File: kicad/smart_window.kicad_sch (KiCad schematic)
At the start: 15 parts, among them J1 PROG, J7 I2C

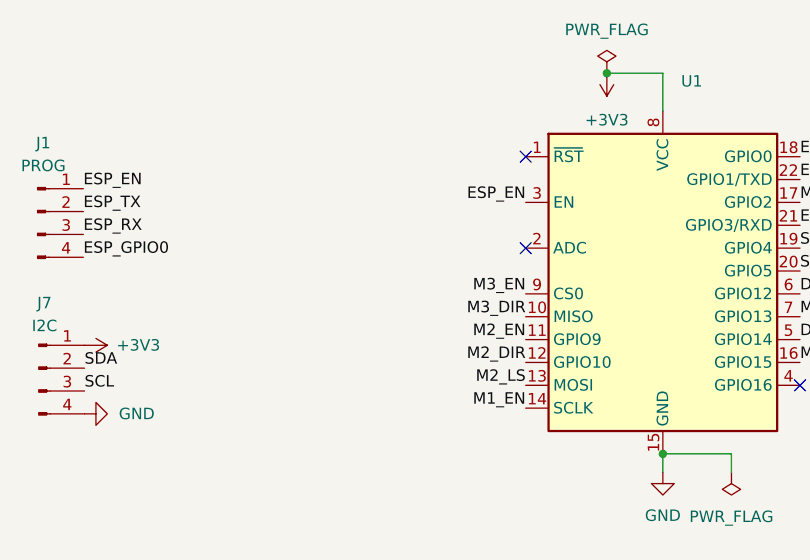
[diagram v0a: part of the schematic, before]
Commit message: добавил фотосенсор
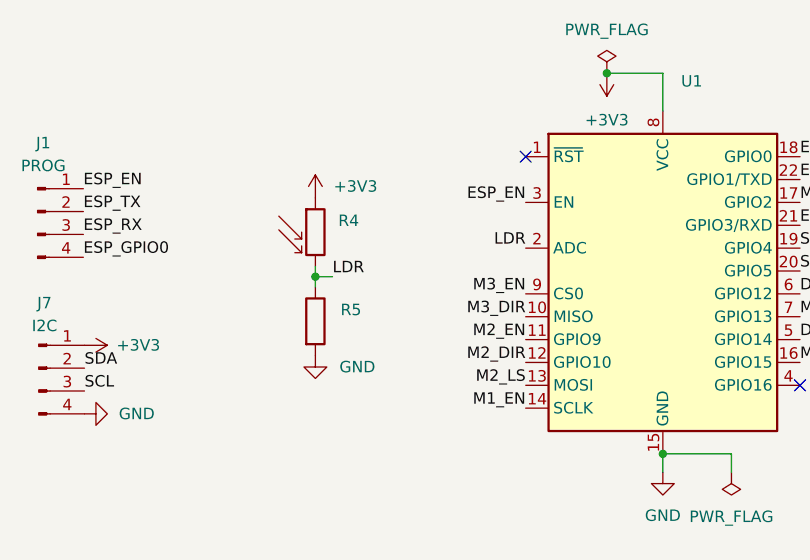
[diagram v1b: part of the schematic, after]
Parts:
- added R4: (no value), symbol Sensor_Optical:A9050
- added R5: (no value), symbol Device:R
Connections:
- net +3V3: now also R4.1
- net GND: now also R5.2
- net LDR: now reaches U1.2 (ADC)
- net LDR: now also R4.2, R5.1
- no-connect marks 3 -> 2
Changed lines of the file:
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@@
 (kicad_sch (version 20211123) (generator eeschema)
   (paper "A4")
+  (junction (at 55.626 46.609) (diameter 0) (color 0 0 0 0)
+  )
   (junction (at 88.011 24.003) (diameter 0) (color 0 0 0 0)
   )
@@
   )
   (no_connect (at 78.994 33.274))
-  (no_connect (at 78.994 43.434))
   (no_connect (at 109.474 58.674))
+  (wire (pts (xy 55.626 45.466) (xy 55.626 46.609))
+    (stroke (width 0) (type default) (color 0 0 0 0))
+  )
   (wire (pts (xy 155.956 50.292) (xy 162.433 50.292))
     (stroke (width 0) (type default) (color 0 0 0 0))
@@
     (stroke (width 0) (type default) (color 0 0 0 0))
   )
+  (wire (pts (xy 55.626 46.609) (xy 55.626 47.752))
+    (stroke (width 0) (type default) (color 0 0 0 0))
+  )
   (wire (pts (xy 124.587 88.519) (xy 128.651 88.519))
     (stroke (width 0) (type default) (color 0 0 0 0))
@@
     (stroke (width 0) (type default) (color 0 0 0 0))
   )
+  (wire (pts (xy 55.626 46.609) (xy 57.531 46.609))
+    (stroke (width 0) (type default) (color 0 0 0 0))
+  )
   (wire (pts (xy 124.587 112.903) (xy 128.651 112.903))
     (stroke (width 0) (type default) (color 0 0 0 0))
@@
     (effects (font (size 1.27 1.27)) (justify right bottom))
   )
+  (label "LDR" (at 57.531 46.609 0)
+    (effects (font (size 1.27 1.27)) (justify left bottom))
+  )
   (label "M2_LS" (at 128.651 97.79 180)
     (effects (font (size 1.27 1.27)) (justify right bottom))
@@
   (label "M1_LS" (at 109.474 56.134 0)
     (effects (font (size 1.27 1.27)) (justify left bottom))
+  )
+  (label "LDR" (at 78.994 43.434 180)
+    (effects (font (size 1.27 1.27)) (justify right bottom))
   )
   (label "M3_LS" (at 109.474 51.054 0)
@@
     )
     (pin "1")
+  )
+  (symbol (lib_id "power:GND") (at 55.626 55.372 0) (unit 1)
+    (in_bom yes) (on_board yes) (fields_autoplaced)
+    (property "Reference" "#PWR011" (id 0) (at 55.626 61.722 0)
+      (effects (font (size 1.27 1.27)) hide)
+    )
+    (property "Value" "GND" (id 1) (at 58.293 56.6419 0)
+      (effects (font (size 1.27 1.27)) (justify left))
+    )
+    (property "Footprint" "" (id 2) (at 55.626 55.372 0)
+      (effects (font (size 1.27 1.27)) hide)
+    )
+    (property "Datasheet" "" (id 3) (at 55.626 55.372 0)
+      (effects (font (size 1.27 1.27)) hide)
+    )
+    (pin "1")
+  )
+  (symbol (lib_id "Device:R") (at 55.626 51.562 0) (unit 1)
+    (in_bom yes) (on_board yes) (fields_autoplaced)
+    (property "Reference" "R5" (id 0) (at 58.42 50.2919 0)
+      (effects (font (size 1.27 1.27)) (justify left))
+    )
+    (property "Value" "" (id 1) (at 58.42 52.8319 0)
+      (effects (font (size 1.27 1.27)) (justify left))
+    )
+    (property "Footprint" "" (id 2) (at 53.848 51.562 90)
+      (effects (font (size 1.27 1.27)) hide)
+    )
+    (property "Datasheet" "~" (id 3) (at 55.626 51.562 0)
+      (effects (font (size 1.27 1.27)) hide)
+    )
+    (pin "1")
+    (pin "2")
   )
   (symbol (lib_id "Connector:Conn_01x02_Male") (at 133.731 110.363 0) (mirror y) (unit 1)
@@
     (pin "2")
   )
+  (symbol (lib_id "power:+3V3") (at 55.626 37.846 0) (unit 1)
+    (in_bom yes) (on_board yes) (fields_autoplaced)
+    (property "Reference" "#PWR08" (id 0) (at 55.626 41.656 0)
+      (effects (font (size 1.27 1.27)) hide)
+    )
+    (property "Value" "+3V3" (id 1) (at 57.658 36.5759 0)
+      (effects (font (size 1.27 1.27)) (justify left))
+    )
+    (property "Footprint" "" (id 2) (at 55.626 37.846 0)
+      (effects (font (size 1.27 1.27)) hide)
+    )
+    (property "Datasheet" "" (id 3) (at 55.626 37.846 0)
+      (effects (font (size 1.27 1.27)) hide)
+    )
+    (pin "1")
+  )
   (symbol (lib_id "Connector:Conn_01x04_Male") (at 24.765 39.37 0) (unit 1)
     (in_bom yes) (on_board yes) (fields_autoplaced)
@@
     (pin "3")
     (pin "4")
+  )
+  (symbol (lib_id "Sensor_Optical:A9050") (at 55.626 41.656 0) (unit 1)
+    (in_bom yes) (on_board yes) (fields_autoplaced)
+    (property "Reference" "R4" (id 0) (at 58.166 40.3859 0)
+      (effects (font (size 1.27 1.27)) (justify left))
+    )
+    (property "Value" "" (id 1) (at 58.166 42.9259 0)
+      (effects (font (size 1.27 1.27)) (justify left))
+    )
+    (property "Footprint" "" (id 2) (at 60.071 41.656 90)
+      (effects (font (size 1.27 1.27)) hide)
+    )
+    (property "Datasheet" "http://cdn-reichelt.de/documents/datenblatt/A500/A90xxxx%23PE.pdf" (id 3) (at 55.626 42.926 0)
+      (effects (font (size 1.27 1.27)) hide)
+    )
+    (pin "1")
+    (pin "2")
   )
   (symbol (lib_id "Connector:Conn_01x02_Male") (at 155.067 20.193 0) (mirror y) (unit 1)
@@
       (reference "#PWR07") (unit 1) (value "GND") (footprint "")
     )
+    (path "/70651bab-fd48-4e85-b84c-55639ba11578"
+      (reference "#PWR08") (unit 1) (value "+3V3") (footprint "")
+    )
     (path "/57e793a7-1996-4f00-92db-a3562d1780dc"
       (reference "#PWR09") (unit 1) (value "GND") (footprint "")
@@
       (reference "#PWR010") (unit 1) (value "GND") (footprint "")
     )
+    (path "/3805e47f-de2b-4f83-86bb-b738762f423a"
+      (reference "#PWR011") (unit 1) (value "GND") (footprint "")
+    )
     (path "/2e774311-d5bd-4ef6-ad7a-5f00d4153613"
       (reference "#PWR014") (unit 1) (value "+3V3") (footprint "")
@@
       (reference "R3") (unit 1) (value "50") (footprint "Resistor_SMD:R_0805_2012Metric")
     )
+    (path "/8407e94d-ce93-4e05-96a2-52621e9e6eb2"
+      (reference "R4") (unit 1) (value "A9050") (footprint "OptoDevice:R_LDR_5.0x4.1mm_P3mm_Vertical")
+    )
+    (path "/3d7ad9f7-d5b6-454d-8f0a-1bda65cbec76"
+      (reference "R5") (unit 1) (value "500") (footprint "Resistor_SMD:R_0805_2012Metric")
+    )
     (path "/c8e0800a-7e51-46cc-9c63-1120638a3624/0d5cf8e3-75e7-46ab-b654-c6274a5de87d"

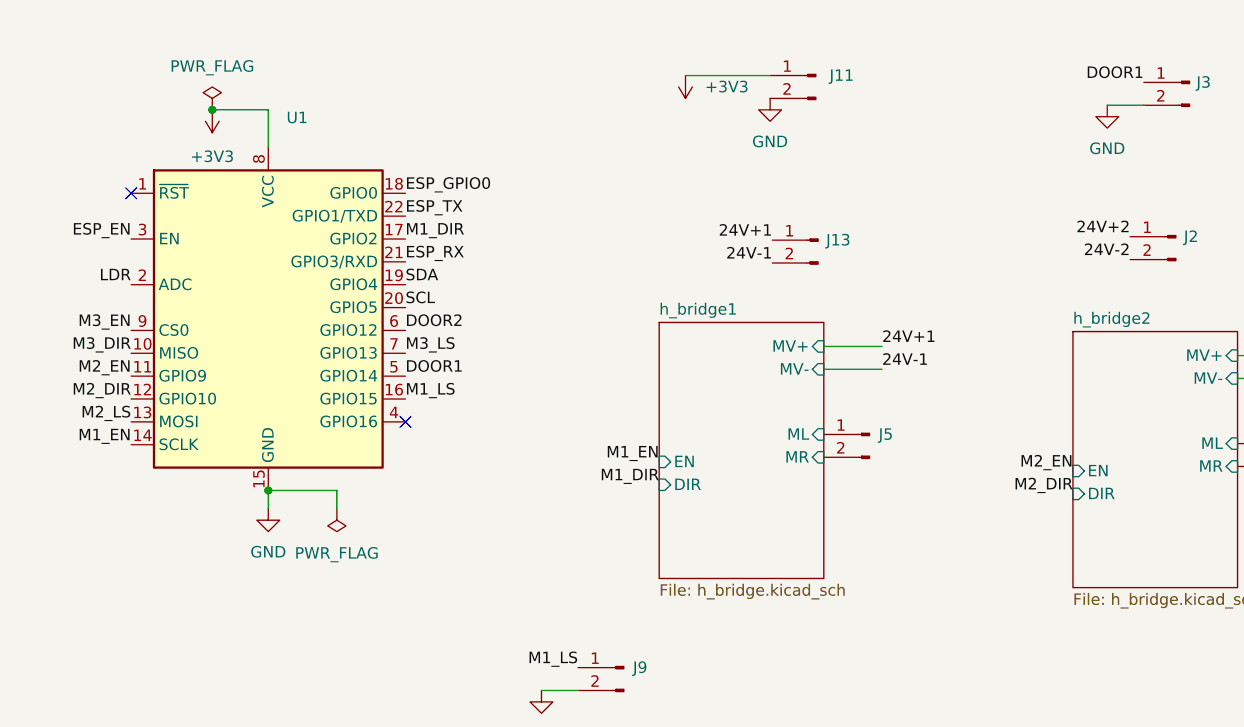
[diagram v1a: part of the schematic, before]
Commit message: добавлен DC-DC преобразователь для питания 3В от БП двигателя
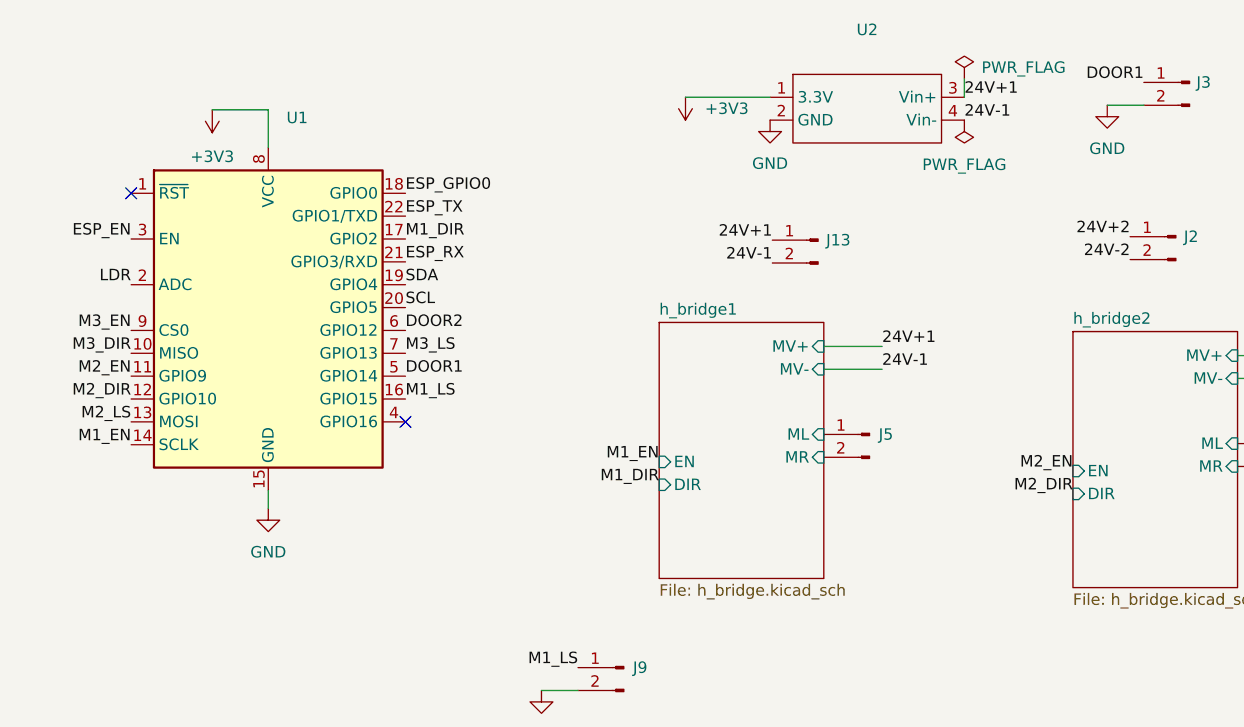
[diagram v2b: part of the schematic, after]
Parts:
- removed J11: (no value), symbol Connector:Conn_01x02_Male
- added U2: (no value), Power Modules:MP1584EN, symbol Power Modules:MP1584EN 3.3V
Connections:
- net +3V3: now also U2.1 (3.3V)
- net 24V+1: now also U2.3 (Vin+)
- net 24V-1: now also U2.4 (Vin-)
- net GND: now also U2.2 (GND)
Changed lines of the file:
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@@
   (junction (at 55.626 46.609) (diameter 0) (color 0 0 0 0)
-  )
-  (junction (at 88.011 24.003) (diameter 0) (color 0 0 0 0)
-  )
-  (junction (at 94.234 66.294) (diameter 0) (color 0 0 0 0)
   )
   (no_connect (at 78.994 33.274))
@@
     (stroke (width 0) (type default) (color 0 0 0 0))
   )
+  (wire (pts (xy 171.577 20.574) (xy 171.577 22.606))
+    (stroke (width 0) (type default) (color 0 0 0 0))
+  )
   (wire (pts (xy 155.956 50.292) (xy 162.433 50.292))
     (stroke (width 0) (type default) (color 0 0 0 0))
@@
     (stroke (width 0) (type default) (color 0 0 0 0))
   )
-  (wire (pts (xy 140.589 20.193) (xy 149.987 20.193))
+  (wire (pts (xy 140.589 22.606) (xy 149.987 22.606))
     (stroke (width 0) (type default) (color 0 0 0 0))
   )
@@
     (stroke (width 0) (type default) (color 0 0 0 0))
   )
-  (wire (pts (xy 101.854 66.294) (xy 94.234 66.294))
-    (stroke (width 0) (type default) (color 0 0 0 0))
-  )
-  (wire (pts (xy 101.854 68.326) (xy 101.854 66.294))
-    (stroke (width 0) (type default) (color 0 0 0 0))
-  )
   (wire (pts (xy 55.626 46.609) (xy 57.531 46.609))
     (stroke (width 0) (type default) (color 0 0 0 0))
@@
   (label "M3_DIR" (at 224.028 66.929 180)
     (effects (font (size 1.27 1.27)) (justify right bottom))
+  )
+  (label "24V+1" (at 171.577 22.606 0)
+    (effects (font (size 1.27 1.27)) (justify left bottom))
+  )
+  (label "24V-1" (at 171.577 25.146 0)
+    (effects (font (size 1.27 1.27)) (justify left bottom))
   )
   (label "LDR" (at 57.531 46.609 0)
@@
     (pin "1")
   )
-  (symbol (lib_id "power:GND") (at 149.987 22.733 0) (unit 1)
-    (in_bom yes) (on_board yes) (fields_autoplaced)
-    (property "Reference" "#PWR017" (id 0) (at 149.987 29.083 0)
-      (effects (font (size 1.27 1.27)) hide)
-    )
-    (property "Value" "GND" (id 1) (at 149.987 27.559 0))
-    (property "Footprint" "" (id 2) (at 149.987 22.733 0)
-      (effects (font (size 1.27 1.27)) hide)
-    )
-    (property "Datasheet" "" (id 3) (at 149.987 22.733 0)
-      (effects (font (size 1.27 1.27)) hide)
-    )
-    (pin "1")
-  )
-  (symbol (lib_id "power:PWR_FLAG") (at 101.854 68.326 180) (unit 1)
-    (in_bom yes) (on_board yes) (fields_autoplaced)
-    (property "Reference" "#FLG0101" (id 0) (at 101.854 70.231 0)
-      (effects (font (size 1.27 1.27)) hide)
-    )
-    (property "Value" "PWR_FLAG" (id 1) (at 101.854 73.279 0))
-    (property "Footprint" "" (id 2) (at 101.854 68.326 0)
-      (effects (font (size 1.27 1.27)) hide)
-    )
-    (property "Datasheet" "~" (id 3) (at 101.854 68.326 0)
+  (symbol (lib_id "power:GND") (at 149.987 25.146 0) (unit 1)
+    (in_bom yes) (on_board yes) (fields_autoplaced)
+    (property "Reference" "#PWR017" (id 0) (at 149.987 31.496 0)
+      (effects (font (size 1.27 1.27)) hide)
+    )
+    (property "Value" "GND" (id 1) (at 149.987 29.972 0))
+    (property "Footprint" "" (id 2) (at 149.987 25.146 0)
+      (effects (font (size 1.27 1.27)) hide)
+    )
+    (property "Datasheet" "" (id 3) (at 149.987 25.146 0)
       (effects (font (size 1.27 1.27)) hide)
     )
@@
     )
     (property "Datasheet" "" (id 3) (at 124.587 88.519 0)
+      (effects (font (size 1.27 1.27)) hide)
+    )
+    (pin "1")
+  )
+  (symbol (lib_id "power:PWR_FLAG") (at 171.577 20.574 0) (unit 1)
+    (in_bom yes) (on_board yes) (fields_autoplaced)
+    (property "Reference" "#FLG0101" (id 0) (at 171.577 18.669 0)
+      (effects (font (size 1.27 1.27)) hide)
+    )
+    (property "Value" "PWR_FLAG" (id 1) (at 173.482 19.3039 0)
+      (effects (font (size 1.27 1.27)) (justify left))
+    )
+    (property "Footprint" "" (id 2) (at 171.577 20.574 0)
+      (effects (font (size 1.27 1.27)) hide)
+    )
+    (property "Datasheet" "~" (id 3) (at 171.577 20.574 0)
       (effects (font (size 1.27 1.27)) hide)
     )
@@
     )
     (pin "1")
+  )
+  (symbol (lib_id "Power Modules:MP1584EN 3.3V") (at 160.147 23.876 0) (unit 1)
+    (in_bom yes) (on_board yes) (fields_autoplaced)
+    (property "Reference" "U2" (id 0) (at 160.782 15.113 0))
+    (property "Value" "" (id 1) (at 160.782 17.653 0))
+    (property "Footprint" "Power Modules:MP1584EN" (id 2) (at 149.987 22.606 0)
+      (effects (font (size 1.27 1.27)) hide)
+    )
+    (property "Datasheet" "https://aliexpress.ru/item/1005003880292594.html" (id 3) (at 160.147 32.766 0)
+      (effects (font (size 1.27 1.27)) hide)
+    )
+    (pin "1")
+    (pin "2")
+    (pin "3")
+    (pin "4")
   )
   (symbol (lib_id "RF_Module:ESP-12F") (at 94.234 48.514 0) (unit 1)
@@
     (pin "2")
   )
-  (symbol (lib_id "Connector:Conn_01x02_Male") (at 155.067 20.193 0) (mirror y) (unit 1)
-    (in_bom yes) (on_board yes) (fields_autoplaced)
-    (property "Reference" "J11" (id 0) (at 156.591 20.1929 0)
-      (effects (font (size 1.27 1.27)) (justify right))
-    )
-    (property "Value" "" (id 1) (at 156.591 22.7329 0)
-      (effects (font (size 1.27 1.27)) (justify right))
-    )
-    (property "Footprint" "" (id 2) (at 155.067 20.193 0)
-      (effects (font (size 1.27 1.27)) hide)
-    )
-    (property "Datasheet" "~" (id 3) (at 155.067 20.193 0)
-      (effects (font (size 1.27 1.27)) hide)
-    )
-    (pin "1")
-    (pin "2")
-  )
   (symbol (lib_id "power:GND") (at 29.972 61.849 90) (unit 1)
     (in_bom yes) (on_board yes) (fields_autoplaced)
@@
     (pin "1")
   )
-  (symbol (lib_id "power:PWR_FLAG") (at 88.011 24.003 0) (unit 1)
-    (in_bom yes) (on_board yes) (fields_autoplaced)
-    (property "Reference" "#FLG01" (id 0) (at 88.011 22.098 0)
-      (effects (font (size 1.27 1.27)) hide)
-    )
-    (property "Value" "PWR_FLAG" (id 1) (at 88.011 19.177 0))
-    (property "Footprint" "" (id 2) (at 88.011 24.003 0)
-      (effects (font (size 1.27 1.27)) hide)
-    )
-    (property "Datasheet" "~" (id 3) (at 88.011 24.003 0)
+  (symbol (lib_id "power:PWR_FLAG") (at 171.577 25.146 180) (unit 1)
+    (in_bom yes) (on_board yes) (fields_autoplaced)
+    (property "Reference" "#FLG0102" (id 0) (at 171.577 27.051 0)
+      (effects (font (size 1.27 1.27)) hide)
+    )
+    (property "Value" "PWR_FLAG" (id 1) (at 171.577 30.099 0))
+    (property "Footprint" "" (id 2) (at 171.577 25.146 0)
+      (effects (font (size 1.27 1.27)) hide)
+    )
+    (property "Datasheet" "~" (id 3) (at 171.577 25.146 0)
       (effects (font (size 1.27 1.27)) hide)
     )
@@
     (pin "2")
   )
-  (symbol (lib_id "power:+3V3") (at 140.589 20.193 180) (unit 1)
+  (symbol (lib_id "power:+3V3") (at 140.589 22.606 180) (unit 1)
     (in_bom yes) (on_board yes)
-    (property "Reference" "#PWR016" (id 0) (at 140.589 16.383 0)
-      (effects (font (size 1.27 1.27)) hide)
-    )
-    (property "Value" "+3V3" (id 1) (at 142.748 21.4629 0)
-      (effects (font (size 1.27 1.27)) (justify right))
-    )
-    (property "Footprint" "" (id 2) (at 140.589 20.193 0)
-      (effects (font (size 1.27 1.27)) hide)
-    )
-    (property "Datasheet" "" (id 3) (at 140.589 20.193 0)
+    (property "Reference" "#PWR016" (id 0) (at 140.589 18.796 0)
+      (effects (font (size 1.27 1.27)) hide)
+    )
+    (property "Value" "+3V3" (id 1) (at 142.748 23.8759 0)
+      (effects (font (size 1.27 1.27)) (justify right))
+    )
+    (property "Footprint" "" (id 2) (at 140.589 22.606 0)
+      (effects (font (size 1.27 1.27)) hide)
+    )
+    (property "Datasheet" "" (id 3) (at 140.589 22.606 0)
       (effects (font (size 1.27 1.27)) hide)
     )
@@
   )
   (symbol_instances
-    (path "/bc9dccb7-f29e-45b0-9679-592bb5c286c7"
-      (reference "#FLG01") (unit 1) (value "PWR_FLAG") (footprint "")
-    )
-    (path "/33104779-36fd-476d-a6d8-6e7021545d3d"
+    (path "/36634bbd-43fa-4289-adf5-4285d5ab34e1"
       (reference "#FLG0101") (unit 1) (value "PWR_FLAG") (footprint "")
+    )
+    (path "/b961c8e0-ab41-4862-99c4-46e1c0c0e0d3"
+      (reference "#FLG0102") (unit 1) (value "PWR_FLAG") (footprint "")
     )
     (path "/365b47e0-7e89-4d0e-a2a3-51f941581df2"
@@
       (reference "J10") (unit 1) (value "LS2") (footprint "Connector_JST:JST_XH_B2B-XH-A_1x02_P2.50mm_Vertical")
     )
-    (path "/8e4d1c15-eb55-492a-bff6-de12fa1aee4f"
-      (reference "J11") (unit 1) (value "Vin") (footprint "Connector_JST:JST_XH_B2B-XH-A_1x02_P2.50mm_Vertical")
-    )
     (path "/40060cdf-6600-441c-adc0-295b4c9b515f"
       (reference "J12") (unit 1) (value "LS3") (footprint "Connector_JST:JST_XH_B2B-XH-A_1x02_P2.50mm_Vertical")
@@
       (reference "U1") (unit 1) (value "ESP-12F") (footprint "RF_Module:ESP-12E")
     )
+    (path "/62c804da-cd33-485d-8883-abaf4b362cfb"
+      (reference "U2") (unit 1) (value "MP1584EN 3.3V") (footprint "Power Modules:MP1584EN")
+    )
     (path "/c8e0800a-7e51-46cc-9c63-1120638a3624/bb55911b-a712-4191-8ac2-8c94d03b798f"
